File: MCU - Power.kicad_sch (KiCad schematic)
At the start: 1 part, among them U1 STM32H743ZIT6TR

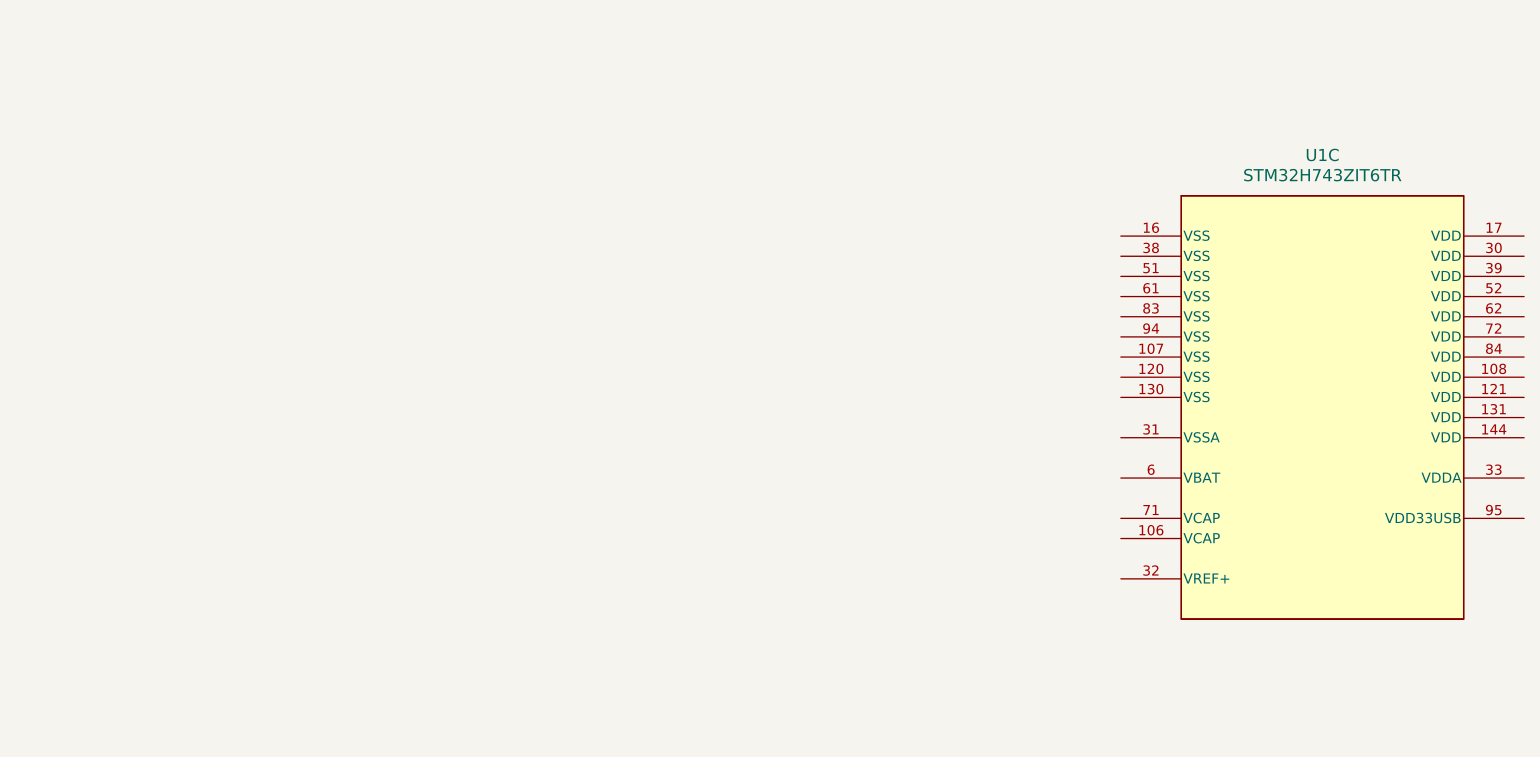
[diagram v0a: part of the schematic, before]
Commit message: charging int and i2c
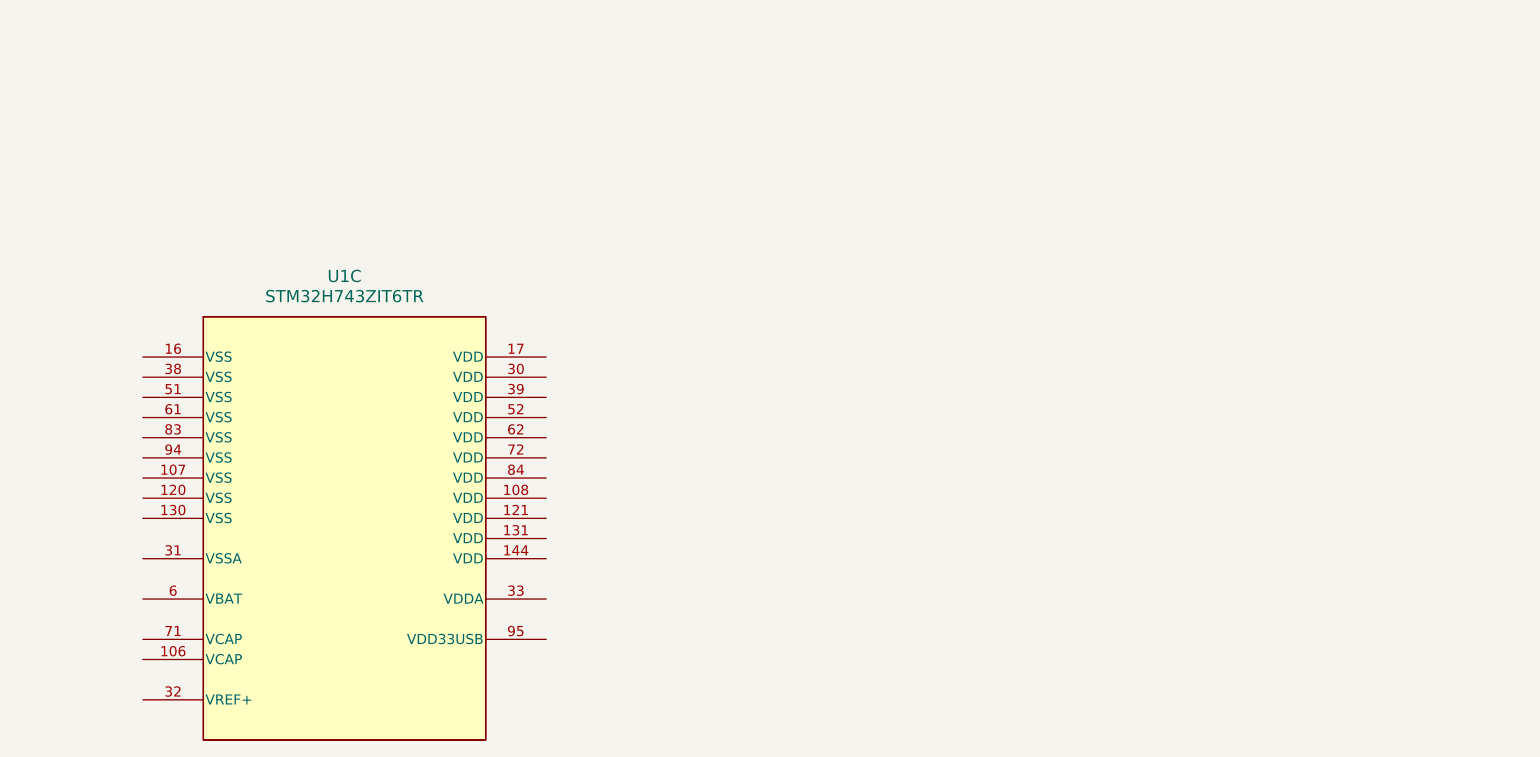
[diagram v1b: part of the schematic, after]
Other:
- moved on the sheet: U1C
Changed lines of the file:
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@@
 	(symbol
 		(lib_id "0_integrated_circuits:STM32H743ZIT6TR")
-		(at 290.83 67.31 0)
+		(at 167.64 82.55 0)
 		(unit 3)
 		(exclude_from_sim no)
@@
 		(fields_autoplaced yes)
 		(property "Reference" "U1"
-			(at 316.23 57.15 0)
+			(at 193.04 72.39 0)
 			(effects
 				(font
@@
 		)
 		(property "Value" "STM32H743ZIT6TR"
-			(at 316.23 59.69 0)
+			(at 193.04 74.93 0)
 			(effects
 				(font
@@
 		)
 		(property "Footprint" "LQFP-144_1_STM"
-			(at 290.83 67.31 0)
+			(at 167.64 82.55 0)
 			(effects
 				(font
@@
 		)
 		(property "Datasheet" "STM32H743ZIT6TR"
-			(at 290.83 67.31 0)
+			(at 167.64 82.55 0)
 			(effects
 				(font
@@
 		)
 		(property "Description" ""
-			(at 290.83 67.31 0)
+			(at 167.64 82.55 0)
 			(effects
 				(font
@@
 		)
 		(property "Supplier 1" "JLCPCB"
-			(at 290.83 67.31 0)
+			(at 167.64 82.55 0)
 			(effects
 				(font
@@
 		)
 		(property "Supplier Part Number 1" "C114408"
-			(at 290.83 67.31 0)
+			(at 167.64 82.55 0)
 			(effects
 				(font

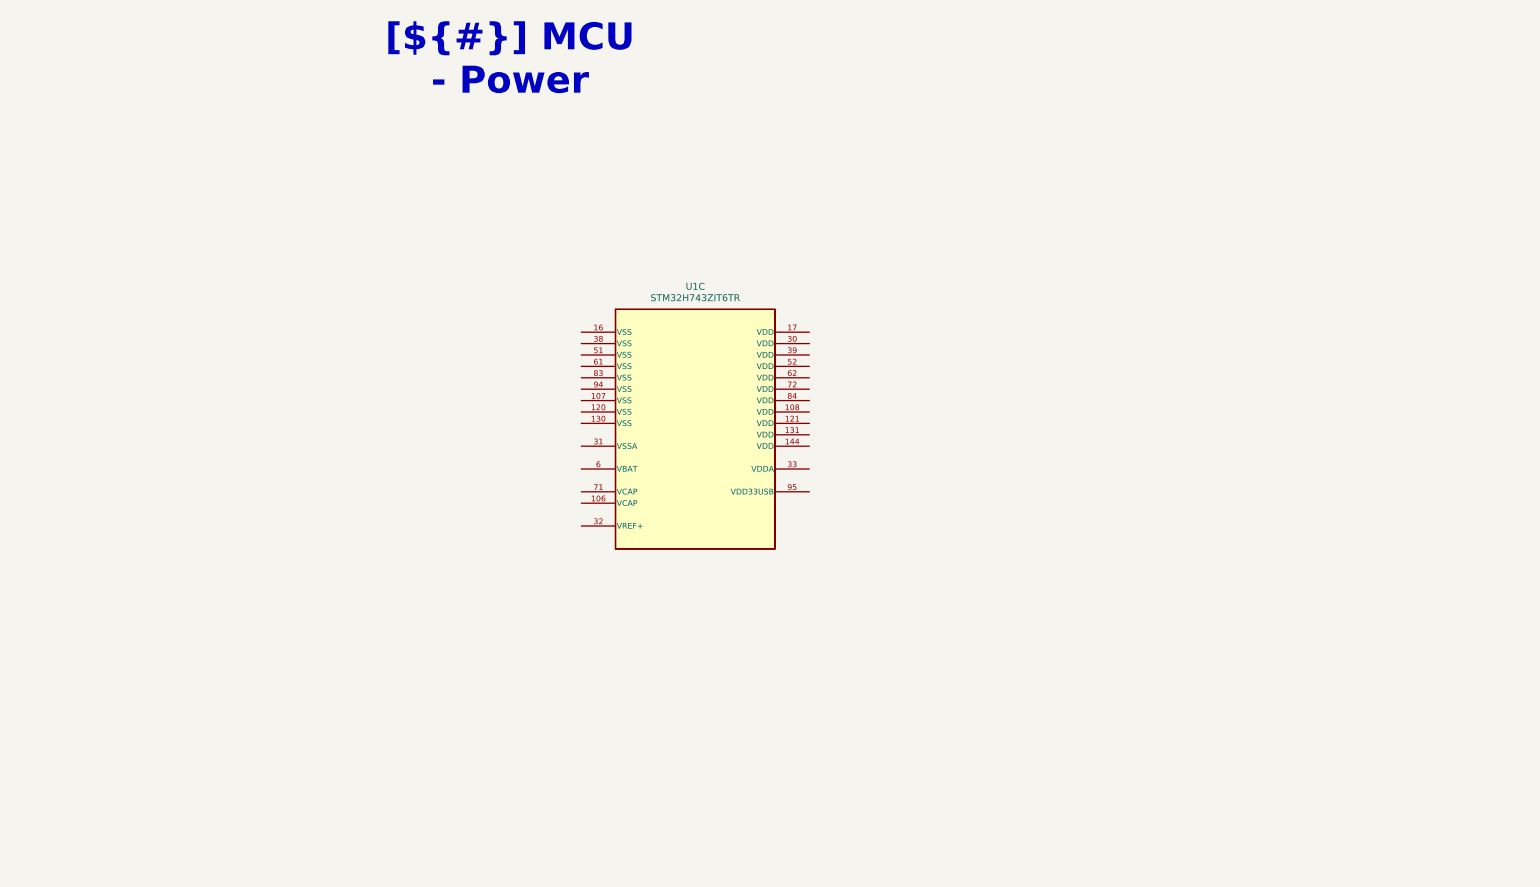
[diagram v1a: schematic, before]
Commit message: added power for mcu
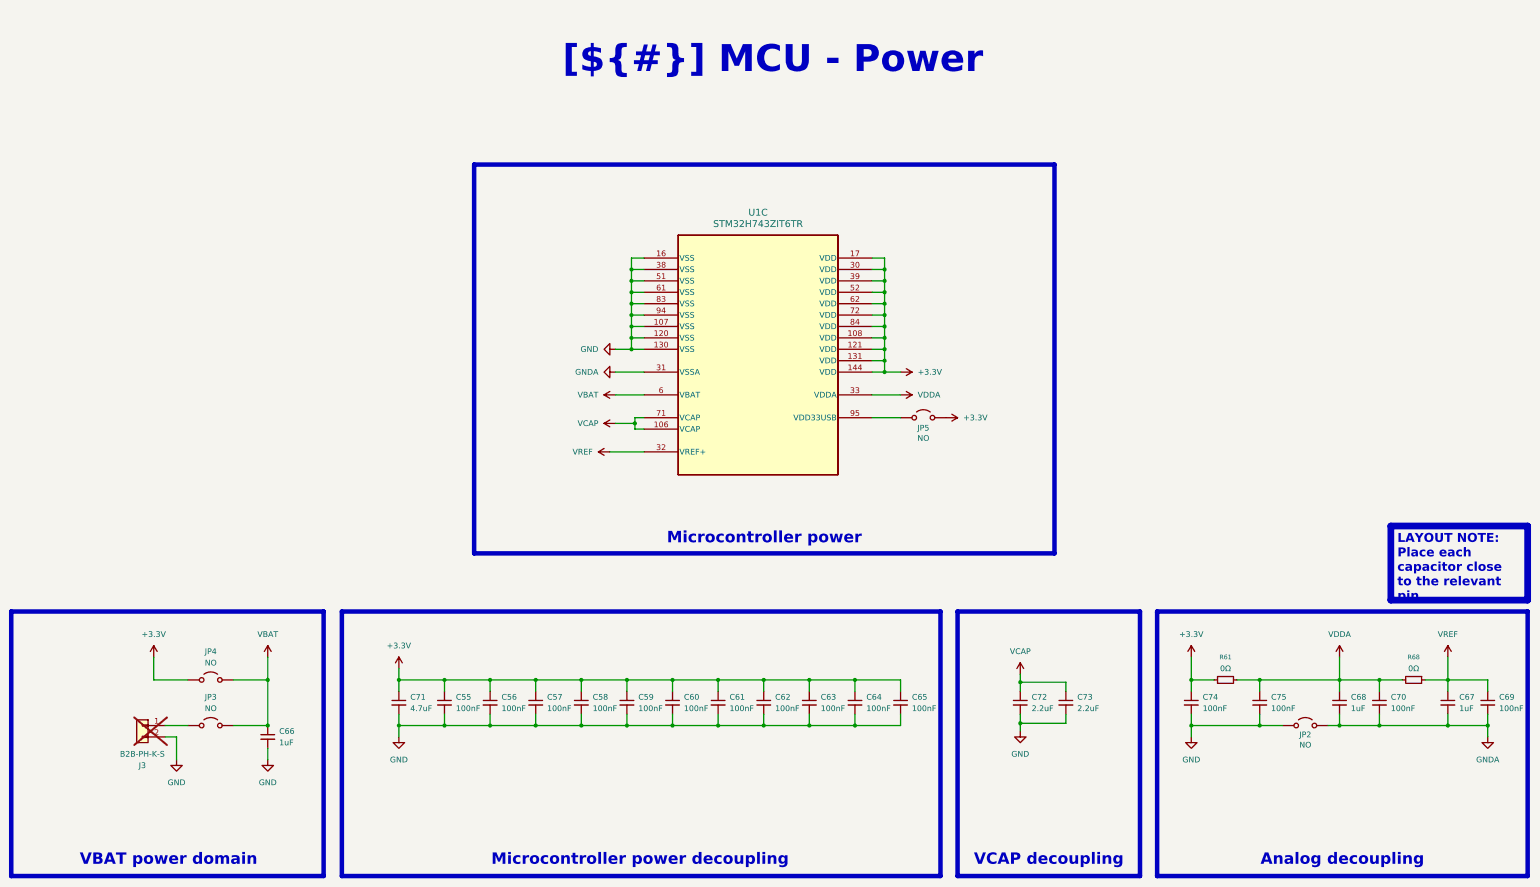
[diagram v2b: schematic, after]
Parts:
- added C55, C56, C57, C58, C59, C60, C61, C62, C63, C64, C65, C69, C70, C74, C75: 100nF, 0_capacitors:C_0402_1005Metric, symbol 0_capacitors:CL05B104KO5NNNC
- added C66, C67, C68: 1uF, 0_capacitors:C_0603_1608Metric, symbol 0_capacitors:CL10A105KB8NNNC
- added C71: 4.7uF, 0_capacitors:C_0805_2012Metric, symbol 0_capacitors:CL21A475KAQNNNE
- added C72, C73: 2.2uF, 0_capacitors:C_1206_3216Metric, symbol 0_capacitors:CL31B225KBHNNNE
- added J3: B2B-PH-K-S, Connector_JST:JST_PH_B2B-PH-K_1x02_P2.00mm_Vertical, symbol 0_connectors:B2B-PH-K-S
- added JP2, JP3, JP4, JP5: NO, Jumper:SolderJumper-2_P1.3mm_Open_TrianglePad1.0x1.5mm, symbol 0_modules:Jumper_2_Open
- added R61, R68: 0Ω, 0_resistors:R_0402_1005Metric, symbol 0_resistors:0402WGF0000TCE
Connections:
- net VCAP: now reaches U1.106 (VCAP)
- net VCAP: now also U1.71 (VCAP), C72.1, C73.1
- net GND: now reaches U1.107 (VSS)
- net GND: now also U1.120 (VSS), U1.130 (VSS), U1.16 (VSS), U1.38 (VSS), U1.51 (VSS), U1.61 (VSS), U1.83 (VSS), U1.94 (VSS), C55.2, C56.2, C57.2, C58.2, C59.2, C60.2, C61.2, C62.2, C63.2, C64.2, C65.2, C66.2, C71.2, C72.2, C73.2, C74.2, C75.2, J3.2 (Pin_2), JP2.1 (A)
- net +3.3V: now reaches U1.108 (VDD)
- net +3.3V: now also U1.121 (VDD), U1.131 (VDD), U1.144 (VDD), U1.17 (VDD), U1.30 (VDD), U1.39 (VDD), U1.52 (VDD), U1.62 (VDD), U1.72 (VDD), U1.84 (VDD), C55.1, C56.1, C57.1, C58.1, C59.1, C60.1, C61.1, C62.1, C63.1, C64.1, C65.1, C71.1, C74.1, JP4.1 (A), JP5.2 (B), R61.1
- net GNDA: now reaches U1.31 (VSSA)
- net GNDA: now also C67.2, C68.2, C69.2, C70.2, JP2.2 (B)
- net VREF: now reaches U1.32 (VREF+)
- net VREF: now also C67.1, C69.1, R68.1
- net VDDA: now reaches U1.33 (VDDA)
- net VDDA: now also C68.1, C70.1, C75.1, R61.2, R68.2
- net VBAT: now reaches U1.6 (VBAT)
- net VBAT: now also C66.1, JP3.2 (B), JP4.2 (B)
- net at U1.95 (VDD33USB): now also JP5.1 (A)
- new net: J3.1 (Pin_1), JP3.1 (A)
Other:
- moved on the sheet: U1C
